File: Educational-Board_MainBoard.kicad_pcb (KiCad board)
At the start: 2 copper layers, 170 x 75 mm, 197 parts, among them J201 Screw_Terminal_01x02_P5mm, J202 USB-C_304A-ACP16X, J401 ACC_INT1, J402 BME_SPI, J403 LUX_INT, J501 RGB_OUT, J601 PWR_IN1, J602 PWR_IN2, J603 PWR_IN3, J604 PWR_IN4, J605 MCP_INT, J606 5V, J607 GND, J608 3V3, J609 EX_PA, J610 EX_PB, J611 PWR_OUT1, J612 PWR_OUT3, J613 PWR_OUT2, J614 PWR_OUT4, Q501 AO3400A, Q601 IRLML9301TRPBF, Q602 IRLML9301TRPBF, Q603 IRLML9301TRPBF, Q604 IRLML9301TRPBF, SW301 RESET, SW501 BUTTON1, SW502 BUTTON2, SW503 BUTTON3, SW504 BUTTON4, SW505 BUTTON5, U201 TPS5430DDA, U202 NUCLEO64-H503RB, U401 LSM6DS3, U402 BME280, U403 OPT4001, U404 INA2180A2, U406 YK16S-L7.2-B10Ka(32-8)-G-A29, U501 74LVC1G34, U502 SSD1315 OLED 0.98", U601 TLP291-4, U602 TLP291-4, U603 MCP23017_SS

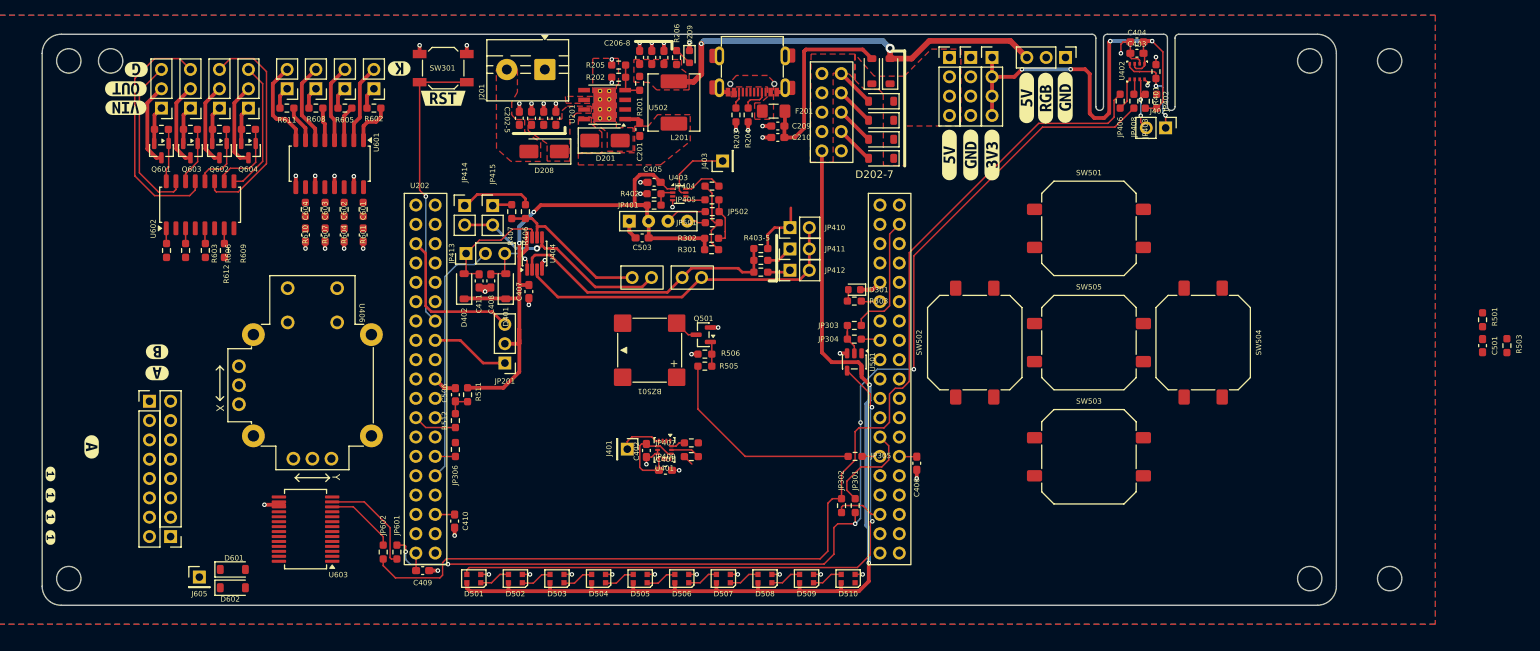
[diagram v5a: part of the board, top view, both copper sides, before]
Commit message: Routed most LEFT part of the board + modified button footprint + fixed some lables
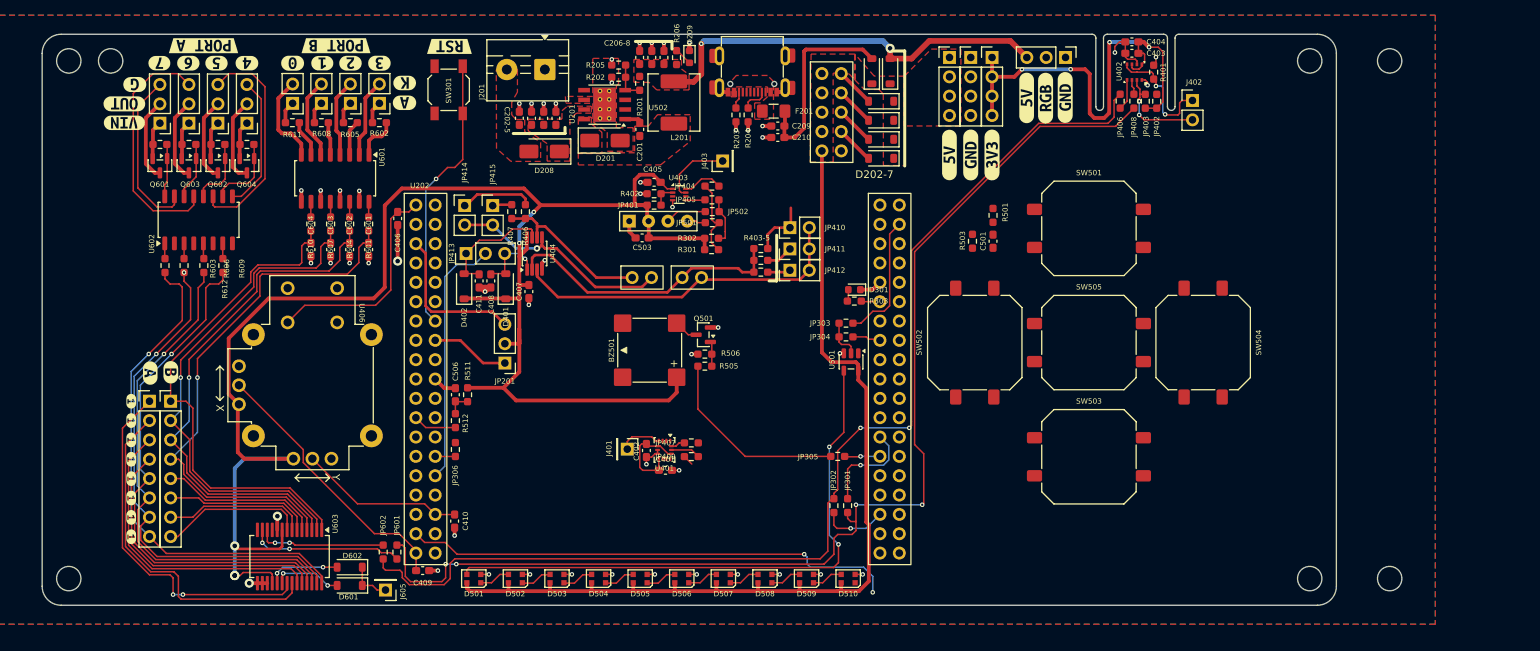
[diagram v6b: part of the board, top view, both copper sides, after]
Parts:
- removed the kibuzzard-69F28E96 at (76.0, 104.2)
- added kibuzzard-69F29536: G***, kibuzzard-69F29536, F.Cu at (81.2, 113.5)
- added kibuzzard-69F29536: G***, kibuzzard-69F29536, F.Cu at (81.2, 116.0)
- added kibuzzard-69F29536: G***, kibuzzard-69F29536, F.Cu at (81.2, 110.9)
- added kibuzzard-69F29536: G***, kibuzzard-69F29536, F.Cu at (81.2, 108.4)
- added kibuzzard-69F9F605: G***, kibuzzard-69F9F605, F.Cu at (90.7, 51.5)
- added kibuzzard-69F9F647: G***, kibuzzard-69F9F647, F.Cu at (113.8, 53.8)
- added kibuzzard-69F9F64C: G***, kibuzzard-69F9F64C, F.Cu at (110.0, 53.8)
- added kibuzzard-69F9F651: G***, kibuzzard-69F9F651, F.Cu at (106.3, 53.8)
- added kibuzzard-69F9F658: G***, kibuzzard-69F9F658, F.Cu at (102.4, 53.8)
- added kibuzzard-69F9F66B: G***, kibuzzard-69F9F66B, F.Cu at (108.1, 51.5)
- added kibuzzard-69F9F712: G***, kibuzzard-69F9F712, F.Cu at (96.4, 53.8)
- added kibuzzard-69F9F718: G***, kibuzzard-69F9F718, F.Cu at (92.4, 53.8)
- added kibuzzard-69F9F71E: G***, kibuzzard-69F9F71E, F.Cu at (88.7, 53.8)
- added kibuzzard-69F9F723: G***, kibuzzard-69F9F723, F.Cu at (84.9, 53.8)
- added kibuzzard-69F9F764: G***, kibuzzard-69F9F764, F.Cu at (117.1, 59.0)
- SW501, SW502, SW503, SW504, SW505: footprint Button_Switch_SMD:SW_Push_1P1T_NO_CK_PTS125Sx43SMTR -> ProjectConnectors:SW_Push_1P1T_NO_CK_PTS125Sx43SMTR
- moved C406 75.4 mm to (116.2, 74.2)
- moved R503 71.5 mm to (191.7, 77.2)
- moved C501 65.7 mm to (194.4, 77.2)
- moved R501 65.7 mm to (194.4, 73.8)
- moved J605 24.5 mm to (114.6, 123.0), turned to 180 degrees
- moved J610 17.8 mm to (86.4, 98.2), turned to 0 degrees
- moved D601 15.6 mm to (109.9, 120.0), turned to 180 degrees
- moved D602 15.5 mm to (109.9, 122.4), turned to 180 degrees
- moved kibuzzard-69F29536 14.8 mm to (81.2, 105.8)
- moved kibuzzard-69F29536 14.7 mm to (81.2, 103.3)
- moved kibuzzard-69F29536 14.4 mm to (81.2, 100.7)
- moved kibuzzard-69F29536 14.3 mm to (81.2, 98.2)
- moved kibuzzard-69F3BF46 6.85 mm to (123.0, 51.6), turned to 180 degrees
- moved J402 5.04 mm to (220.6, 58.7), turned to 0 degrees
- moved U603 4.17 mm to (102.0, 118.6), turned to -90 degrees
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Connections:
- U202 pad 1: /MCU/BTN_3 -> /MCU/JOYSTICK_BTN
- U202 pad 66: /MCU/JOYSTICK_BTN -> /MCU/BTN_3
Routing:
- net +3V3: track 158.6 -> 302.7 mm, vias 6 -> 9
- net /POWER_UI/PB3: track 0.00 -> 71.2 mm, vias 0 -> 1
- net /POWER_UI/PB2: track 0.00 -> 68.5 mm, vias 0 -> 1
- net /POWER_UI/PA4: track 0.00 -> 67.5 mm, vias 0 -> 1
- net /POWER_UI/PB1: track 0.00 -> 66.9 mm, vias 0 -> 1
- net /POWER_UI/PB0: track 0.00 -> 66.1 mm
- net /POWER_UI/PA5: track 0.00 -> 66.0 mm, vias 0 -> 1
- net /POWER_UI/PA6: track 0.00 -> 66.0 mm, vias 0 -> 2
- net /POWER_UI/PA7: track 0.00 -> 65.8 mm, vias 0 -> 1
- net /MCU/BTN_1: track 0.00 -> 65.0 mm, vias 0 -> 2
- net /POWER_UI/PA0: track 0.00 -> 47.3 mm, vias 0 -> 2
- net /POWER_UI/PA1: track 0.00 -> 45.8 mm
- net /POWER_UI/PA2: track 0.00 -> 39.8 mm
- net /POWER_UI/PA3: track 0.00 -> 37.4 mm
- net /MCU/JOYSTICK_X: track 2.32 -> 35.9 mm
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
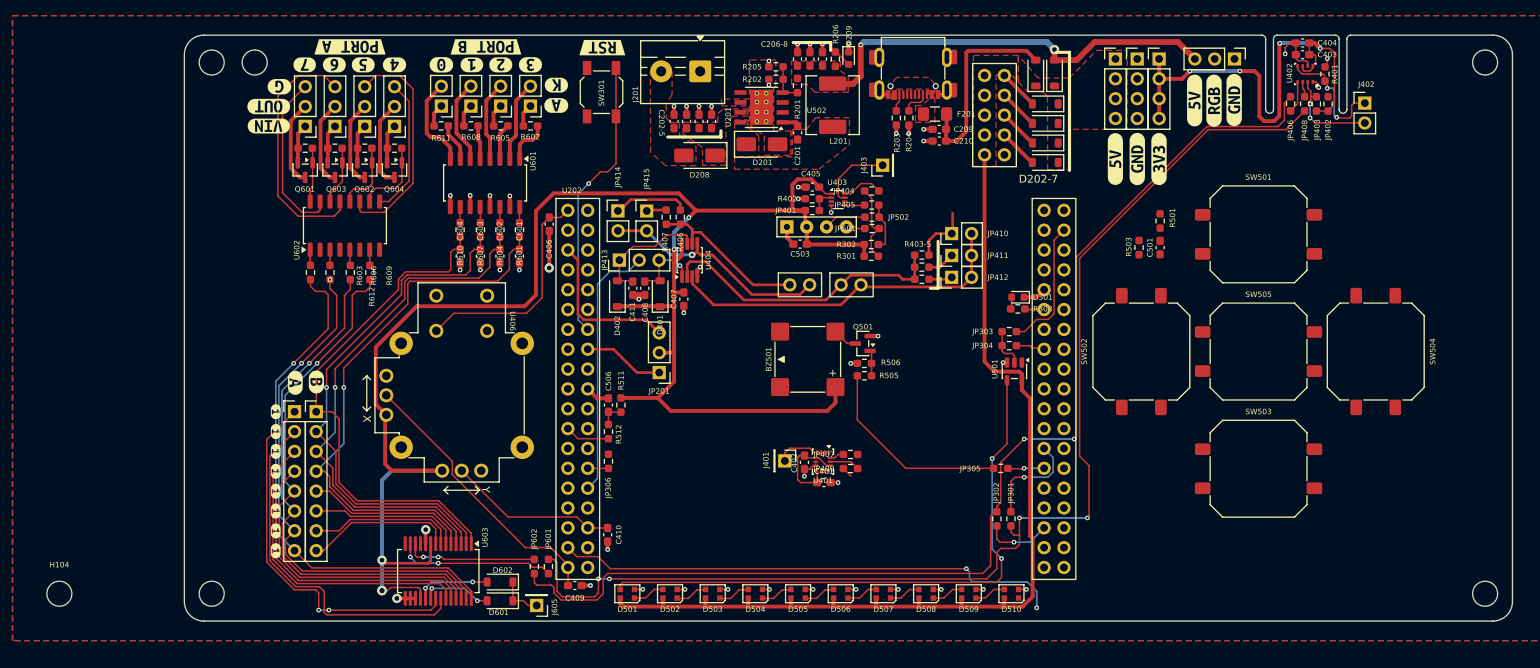
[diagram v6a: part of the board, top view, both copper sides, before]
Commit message: Resized the board at the left part
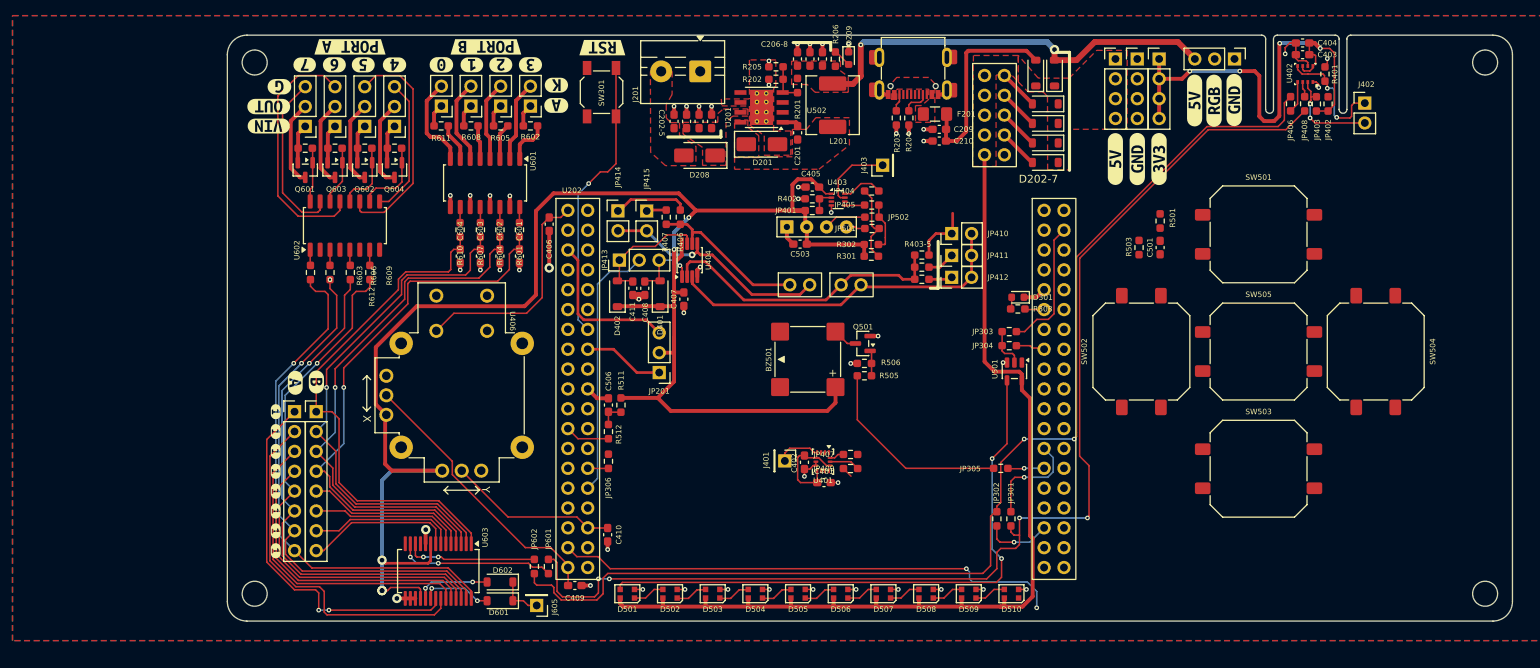
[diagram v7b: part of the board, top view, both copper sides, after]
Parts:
- removed the H101 at (73.0, 53.5)
- removed the H104 at (53.5, 121.5)
- moved H104 5.50 mm to (78.5, 121.5)
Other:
- board size 170 x 75 mm -> 164.5 x 75 mm
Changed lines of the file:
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@@
 				(font
 					(size 0.001 0.001)
+					(thickness 0.15)
 				)
 			)
@@
 				(font
 					(size 0.001 0.001)
+					(thickness 0.15)
 				)
 			)
@@
 		)
 	)
-	(footprint "MountingHole:MountingHole_3.2mm_M3_ISO14580"
-		(layer "F.Cu")
-		(at 53.5 121.5)
-		(descr "Mounting Hole 3.2mm, M3, no annular, generated by kicad-footprint-generator mountinghole.py")
-		(tags "mountinghole M3 ISO14580")
-		(property "Reference" "H104"
-			(at 0 -3.7 0)
-			(layer "F.SilkS")
-			(effects
-				(font
-					(size 0.7 0.7)
-					(thickness 0.15)
-				)
-			)
-		)
-		(property "Value" "MountingHole"
-			(at 0 3.7 0)
-			(layer "F.Fab")
-			(effects
-				(font
-					(size 1 1)
-					(thickness 0.15)
-				)
-			)
-		)
-		(property "Datasheet" "~"
-			(at 0 0 0)
-			(layer "F.Fab")
-			(hide yes)
-			(effects
-				(font
-					(size 1.27 1.27)
-					(thickness 0.15)
-				)
-			)
-		)
-		(property "Description" "Mounting Hole without connection"
-			(at 0 0 0)
-			(layer "F.Fab")
-			(hide yes)
-			(effects
-				(font
-					(size 1.27 1.27)
-					(thickness 0.15)
-				)
-			)
-		)
-		(property "Checked" "OK"
-			(at 0 0 0)
-			(unlocked yes)
-			(layer "F.Fab")
-			(hide yes)
-			(effects
-				(font
-					(size 1 1)
-					(thickness 0.15)
-				)
-			)
-		)
-		(property ki_fp_filters "MountingHole*")
-		(sheetname "/")
-		(sheetfile "Educational-Board_MainBoard.kicad_sch")
-		(attr exclude_from_pos_files exclude_from_bom)
-		(fp_circle
-			(center 0 0)
-			(end 2.75 0)
-			(stroke
-				(width 0.15)
-				(type solid)
-			)
-			(fill no)
-			(layer "Cmts.User")
-		)
-		(fp_circle
-			(center 0 0)
-			(end 3 0)
-			(stroke
-				(width 0.05)
-				(type solid)
-			)
-			(fill no)
-			(layer "F.CrtYd")
-		)
-		(fp_text user "${REFERENCE}"
-			(at 0 0 0)
-			(layer "F.Fab")
-			(effects
-				(font
-					(size 0.7 0.7)
-					(thickness 0.15)
-				)
-			)
-		)
-		(pad "" np_thru_hole circle
-			(at 0 0)
-			(size 3.2 3.2)
-			(drill 3.2)
-			(layers "*.Cu" "*.Mask")
-		)
-		(embedded_fonts no)
-	)
 	(footprint "Resistor_SMD:R_0603_1608Metric_Pad0.98x0.95mm_HandSolder"
 		(layer "F.Cu")
@@
 				(font
 					(size 0.001 0.001)
+					(thickness 0.15)
 				)
 			)
@@
 				(font
 					(size 0.001 0.001)
+					(thickness 0.15)
 				)
 			)
@@
 			(fill yes)
 			(layer "F.SilkS")
-			(net 113064500)
 		)
 		(embedded_fonts no)
@@
 	(footprint "MountingHole:MountingHole_3.2mm_M3_ISO14580"
 		(layer "F.Cu")
-		(at 73 121.5)
+		(at 78.5 121.5)
 		(descr "Mounting Hole 3.2mm, M3, no annular, generated by kicad-footprint-generator mountinghole.py")
 		(tags "mountinghole M3 ISO14580")
@@
 				(font
 					(size 0.001 0.001)
+					(thickness 0.15)
 				)
 			)
@@
 				(font
 					(size 0.001 0.001)
+					(thickness 0.15)
 				)
 			)
@@
 				(font
 					(size 0.001 0.001)
+					(thickness 0.15)
 				)
 			)
@@
 				(font
 					(size 0.001 0.001)
+					(thickness 0.15)
 				)
 			)
@@
 				(font
 					(size 0.001 0.001)
+					(thickness 0.15)
 				)
 			)
@@
 				(font
 					(size 0.001 0.001)
+					(thickness 0.15)
 				)
 			)
@@
 				(font
 					(size 0.001 0.001)
+					(thickness 0.15)
 				)
 			)
@@
 				(font
 					(size 0.001 0.001)
+					(thickness 0.15)
 				)
 			)
@@
 				(font
 					(size 0.001 0.001)
+					(thickness 0.15)
 				)
 			)
@@
 				(font
 					(size 0.001 0.001)
+					(thickness 0.15)
 				)
 			)
@@
 				(font
 					(size 0.001 0.001)
+					(thickness 0.15)
 				)
 			)
@@
 				(font
 					(size 0.001 0.001)
+					(thickness 0.15)
 				)
 			)
@@
 				(font
 					(size 0.001 0.001)
+					(thickness 0.15)
 				)
 			)
@@
 				(font
 					(size 0.001 0.001)
+					(thickness 0.15)
 				)
 			)
@@
 		(embedded_fonts no)
 	)
-	(footprint "MountingHole:MountingHole_3.2mm_M3_ISO14580"
-		(layer "F.Cu")
-		(at 73 53.5)
-		(descr "Mounting Hole 3.2mm, M3, no annular, generated by kicad-footprint-generator mountinghole.py")
-		(tags "mountinghole M3 ISO14580")
-		(property "Reference" "H101"
-			(at 0 -3.7 0)
-			(layer "F.SilkS")
-			(hide yes)
-			(effects
-				(font
-					(size 0.7 0.7)
-					(thickness 0.15)
-				)
-			)
-		)
-		(property "Value" "MountingHole"
-			(at 0 3.7 0)
-			(layer "F.Fab")
-			(effects
-				(font
-					(size 1 1)
-					(thickness 0.15)
-				)
-			)
-		)
-		(property "Datasheet" "~"
-			(at 0 0 0)
-			(layer "F.Fab")
-			(hide yes)
-			(effects
-				(font
-					(size 1.27 1.27)
-					(thickness 0.15)
-				)
-			)
-		)
-		(property "Description" "Mounting Hole without connection"
-			(at 0 0 0)
-			(layer "F.Fab")
-			(hide yes)
-			(effects
-				(font
-					(size 1.27 1.27)
-					(thickness 0.15)
-				)
-			)
-		)
-		(property "Checked" "OK"
-			(at 0 0 0)
-			(unlocked yes)
-			(layer "F.Fab")
-			(hide yes)
-			(effects
-				(font
-					(size 1 1)
-					(thickness 0.15)
-				)
-			)
-		)
-		(attr exclude_from_pos_files exclude_from_bom)
-		(fp_circle
-			(center 0 0)
-			(end 2.75 0)
-			(stroke
-				(width 0.15)
-				(type solid)
-			)
-			(fill no)
-			(layer "Cmts.User")
-		)
-		(fp_circle
-			(center 0 0)
-			(end 3 0)
-			(stroke
-				(width 0.05)
-				(type solid)
-			)
-			(fill no)
-			(layer "F.CrtYd")
-		)
-		(fp_text user "${REFERENCE}"
-			(at 0 0 0)
-			(layer "F.Fab")
-			(effects
-				(font
-					(size 0.7 0.7)
-					(thickness 0.15)
-				)
-			)
-		)
-		(pad "" np_thru_hole circle
-			(at 0 0)
-			(size 3.2 3.2)
-			(drill 3.2)
-			(layers "*.Cu" "*.Mask")
-		)
-		(embedded_fonts no)
-	)
 	(footprint "Resistor_SMD:R_0603_1608Metric_Pad0.98x0.95mm_HandSolder"
 		(layer "F.Cu")
@@
 			(fill yes)
 			(layer "F.SilkS")
-			(net 113064500)
 		)
 		(embedded_fonts no)
@@
 			(fill yes)
 			(layer "F.SilkS")
-			(net 113064500)
 		)
 		(embedded_fonts no)
@@
 			(fill yes)
 			(layer "F.SilkS")
-			(net 113064500)
 		)
 		(embedded_fonts no)
@@
 				(font
 					(size 0.001 0.001)
+					(thickness 0.15)
 				)
 			)
@@
 				(font
 					(size 0.001 0.001)
+					(thickness 0.15)
 				)
 			)
@@
 	)
 	(gr_line
-		(start 69.5 52.5)
-		(end 69.5 122.5)
+		(start 75 52.5)
+		(end 75 122.5)
 		(stroke
 			(width 0.05)
@@
 	)
 	(gr_arc
-		(start 69.5 52.5)
-		(mid 70.232233 50.732233)
-		(end 72 50)
+		(start 75 52.5)
+		(mid 75.732233 50.732233)
+		(end 77.5 50)
 		(stroke
 			(width 0.05)
@@
 	)
 	(gr_arc
-		(start 72 125)
-		(mid 70.232233 124.267767)
-		(end 69.5 122.5)
+		(start 77.5 125)
+		(mid 75.732233 124.267767)
+		(end 75 122.5)
 		(stroke
 			(width 0.05)
@@
 	)
 	(gr_line
-		(start 72 125)
+		(start 77.5 125)
 		(end 237 125)
 		(stroke
@@
 	(gr_line
 		(start 207.4094 50)
-		(end 72 50)
+		(end 77.5 50)
 		(stroke
 			(width 0.05)
@@
 	)
 	(gr_line
-		(start 70 125)
-		(end 70 50)
+		(start 69.5 52.5)
+		(end 69.5 122.5)
+		(stroke
+			(width 0.05)
+			(type default)
+		)
+		(layer "User.1")
+	)
+	(gr_arc
+		(start 69.5 52.5)
+		(mid 70.232233 50.732233)
+		(end 72 50)
 		(stroke
 			(width 0.05)
@@
 		(layer "User.1")
 	)
-	(gr_line
-		(start 76.2 75.6)
-		(end 76.2 117.8)
+	(gr_arc
+		(start 72 125)
+		(mid 70.232233 124.267767)
+		(end 69.5 122.5)
 		(stroke
-			(width 0.1)
-			(type default)
+			(width 0.05)
+			(type solid)
 		)
 		(layer "User.1")
@@
 	)
 	(gr_rect
-		(start 50 50)
-		(end 250 125)
+		(start 69.5 50)
+		(end 239.5 125)
 		(stroke
 			(width 0.05)
@@
 	)
 	(gr_rect
-		(start 69.5 50)
-		(end 239.5 125)
+		(start 75 50)
+		(end 250 125)
 		(stroke
 			(width 0.05)
